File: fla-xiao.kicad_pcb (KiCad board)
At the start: 2 copper layers, 31 x 50 mm, 9 parts, among them J1 Conn_PinHeader_1x08_P2.54mm_V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, J2 Conn_PinHeader_1x04_P2.54mm_V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, J3 Conn_PinHeader_2x03_P2.54mm_V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, SW1 BUTTON_B3SN, U1 MOUDLE-SEEEDUINO-XIAO-ESP32C3

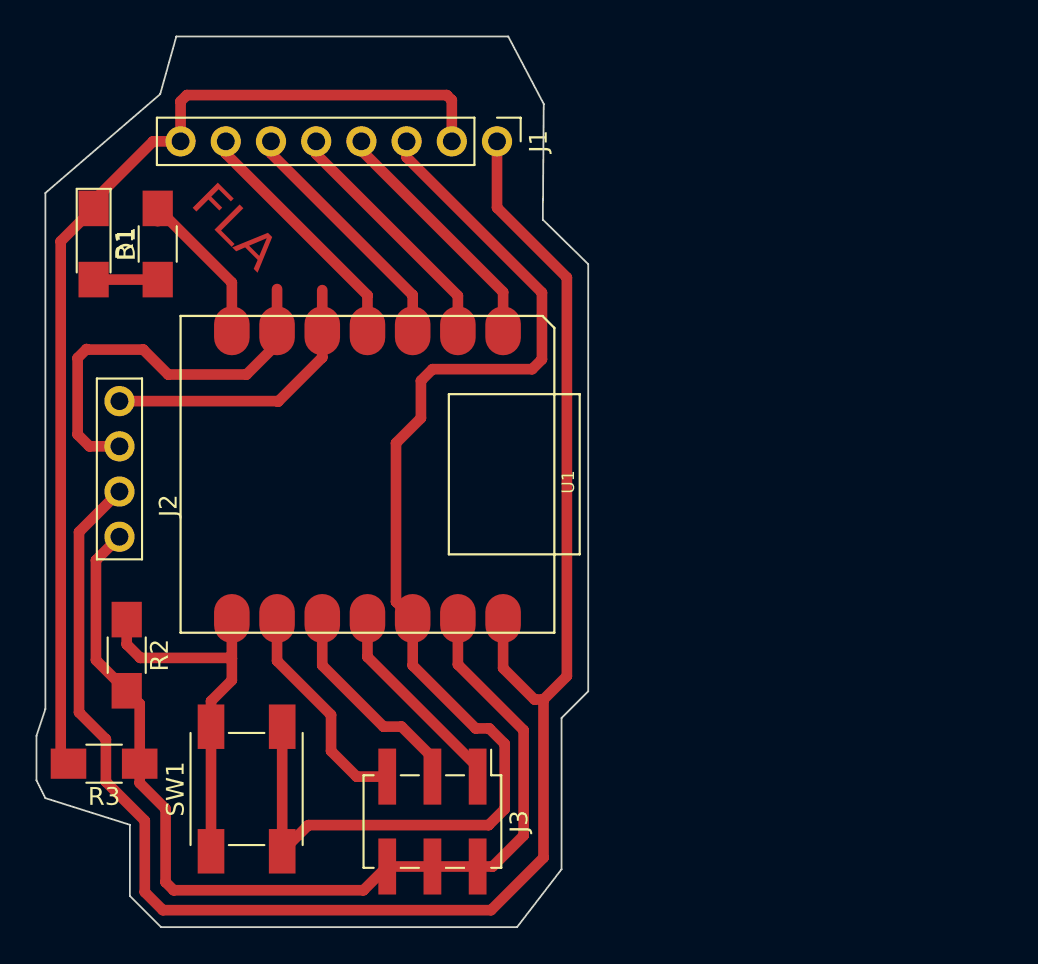
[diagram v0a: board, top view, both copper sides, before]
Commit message: Updated to use sockets with XIAO
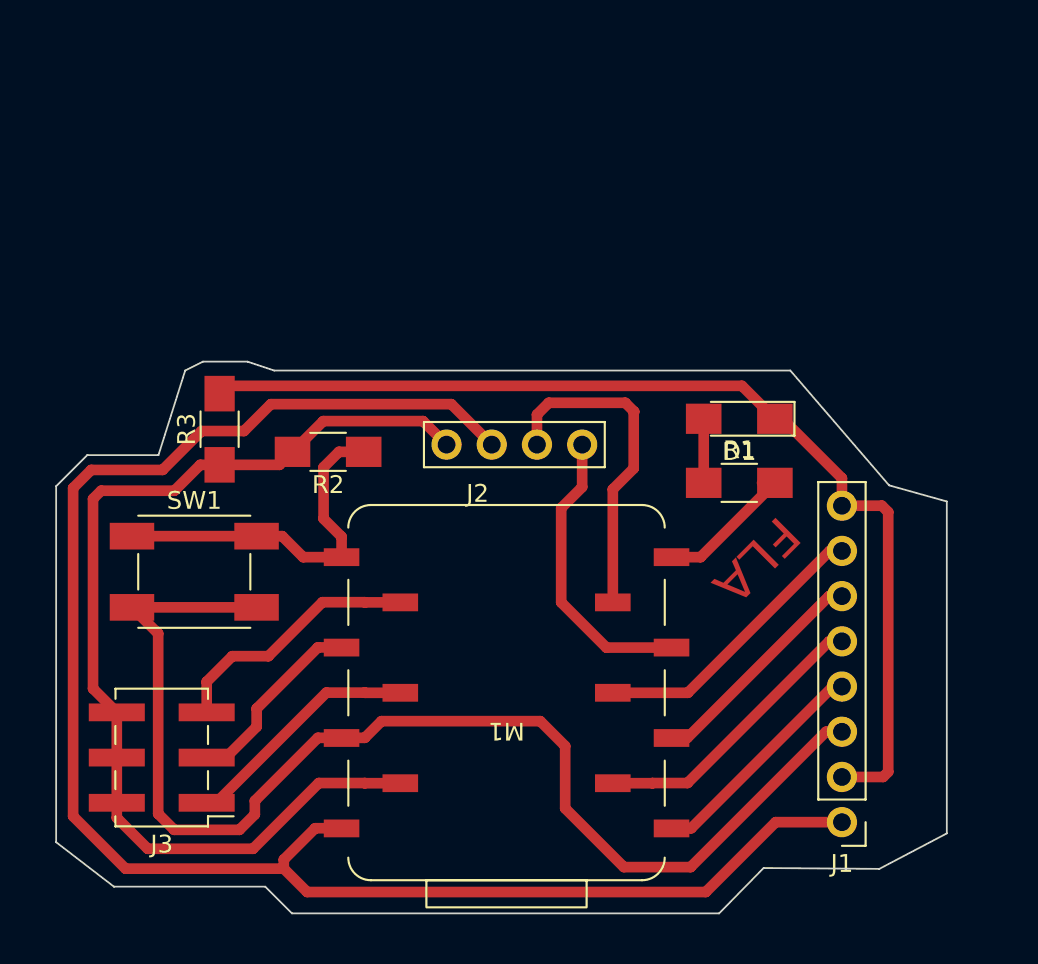
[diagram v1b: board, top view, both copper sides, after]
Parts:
- removed U1: MOUDLE-SEEEDUINO-XIAO-ESP32C3, xiao ESP32C3_PCB:MOUDLE14P-SMD-2.54-21X17.8MM
- added M1: Module_XIAO-RP2040_SocketSMD, fab:SeeedStudio_XIAO_SocketSMD, F.Cu at (148.2, 154.8)
- moved J1 42.9 mm to (167.0, 162.1), turned to 180 degrees
- moved D1 37.6 mm to (161.3, 139.4), turned to 180 degrees
- moved R1 35.3 mm to (161.3, 143.0), turned to 0 degrees
- moved J2 26.1 mm to (152.4, 140.9), turned to -90 degrees
- moved R3 19.9 mm to (132.1, 140.0), turned to 90 degrees
- moved R2 16.1 mm to (138.2, 141.3), turned to 180 degrees
- moved J3 15.6 mm to (128.8, 158.5), turned to 180 degrees
- moved SW1 12.6 mm to (130.6, 148.0), turned to 0 degrees
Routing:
- net Net-(J2-Pin_2): track 22.7 -> 18.8 mm
- net Net-(J1-Pin_5): track 13.9 -> 16.2 mm
- net Net-(J1-Pin_7): track 13.9 -> 16.2 mm
- net Net-(J3-Pin_5): track 12.5 -> 14.5 mm
- net Net-(J3-Pin_1): track 11.4 -> 13.4 mm
- net GND: track 115.8 -> 117.8 mm
- net Net-(J3-Pin_3): track 12.0 -> 10.7 mm
- net +5V: track 97.2 -> 95.9 mm
- net +3V3: track 70.8 -> 69.6 mm
- net Net-(M1-D6): track 9.32 -> 8.26 mm
- net Net-(J1-Pin_4): track 13.9 -> 12.9 mm
- net Net-(M1-D7): track 21.2 -> 20.3 mm
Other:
- board size 31 x 50 mm -> 50 x 31 mm

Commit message: .\fla-xiao.kicad*
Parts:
- moved R1 0.63 mm to (161.3, 142.4)
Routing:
- net Net-(D1-A): track 3.60 -> 2.97 mm

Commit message: Updated board
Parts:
- removed J1: Conn_PinHeader_1x08_P2.54mm_Vertical_THT_D1mm, fab:PinHeader_1x08_P2.54mm_Vertical_THT_D1mm
- removed J2: Conn_PinHeader_1x04_P2.54mm_Vertical_THT_D1mm, fab:PinHeader_1x04_P2.54mm_Vertical_THT_D1mm
- added J4: Conn_PinHeader_1x08_P2.54mm_Horizontal_SMD, fab:PinHeader_1x08_P2.54mm_Horizontal_SMD, F.Cu at (132.7, 147.6)
- added J5: Conn_PinHeader_1x05_P2.54mm_Horizontal_SMD, fab:PinHeader_1x05_P2.54mm_Horizontal_SMD, F.Cu at (155.6, 150.5)
- moved J3 47.8 mm to (169.5, 133.5), turned to 0 degrees
- moved SW1 39.3 mm to (169.7, 144.0)
- moved R3 38.1 mm to (168.3, 152.0), turned to -90 degrees
- moved D1 25.8 mm to (139.1, 152.6), turned to 0 degrees
- moved R2 25.8 mm to (162.2, 150.7)
- moved R1 23.3 mm to (139.1, 149.6), turned to 180 degrees
- moved M1 18.1 mm to (152.1, 137.2), turned to 0 degrees
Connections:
- net +3V3 renamed PWR_3V3
- net Net-(J3-Pin_1) renamed A10
- net Net-(J3-Pin_3) renamed A9
- net Net-(J3-Pin_5) renamed A8
- net Net-(M1-D6) renamed A6
- net Net-(M1-D7) renamed A7
- M1 pad 1: Net-(J1-Pin_4) -> A0
- M1 pad 14: +5V -> PWR_5V
- M1 pad 2: Net-(J1-Pin_5) -> A1
- M1 pad 3: Net-(J1-Pin_6) -> A2
- M1 pad 4: Net-(J1-Pin_7) -> A3
- M1 pad 5: Net-(J2-Pin_1) -> SDA
- M1 pad 6: Net-(J2-Pin_2) -> SCL
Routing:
- net +5V: track 96.0 -> 0.00 mm
- net PWR_5V: track 0.00 -> 54.0 mm
- net PWR_3V3: track 69.6 -> 113.3 mm
- net Net-(J2-Pin_2): track 18.8 -> 0.00 mm
- net A1: track 0.00 -> 16.7 mm
- net A3: track 0.00 -> 16.7 mm
- net Net-(J2-Pin_1): track 16.6 -> 0.00 mm
- net SDA: track 0.00 -> 16.4 mm
- net Net-(J1-Pin_5): track 16.2 -> 0.00 mm
- net Net-(J1-Pin_7): track 16.2 -> 0.00 mm
- net Net-(J1-Pin_6): track 13.6 -> 0.00 mm
- net A0: track 0.00 -> 13.4 mm
- net A2: track 0.00 -> 13.4 mm
- net Net-(J1-Pin_4): track 12.9 -> 0.00 mm
- net SCL: track 0.00 -> 8.98 mm
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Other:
- board size 50 x 31 mm -> 49.7 x 30.7 mm

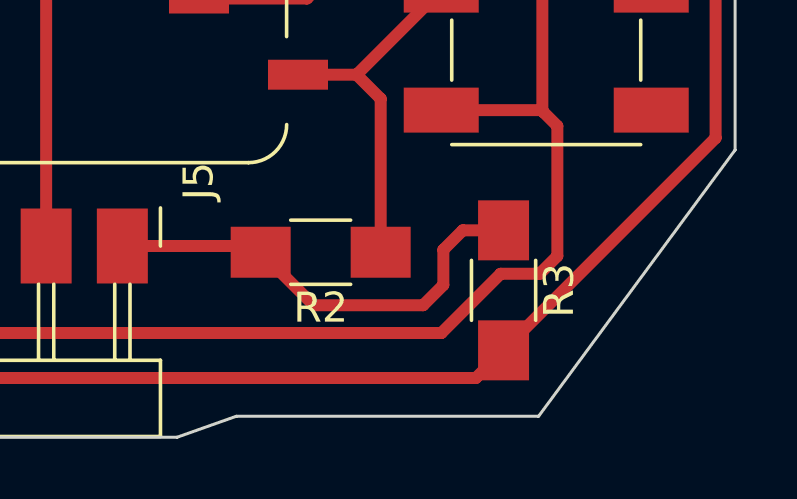
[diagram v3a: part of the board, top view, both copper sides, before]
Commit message: Updated images
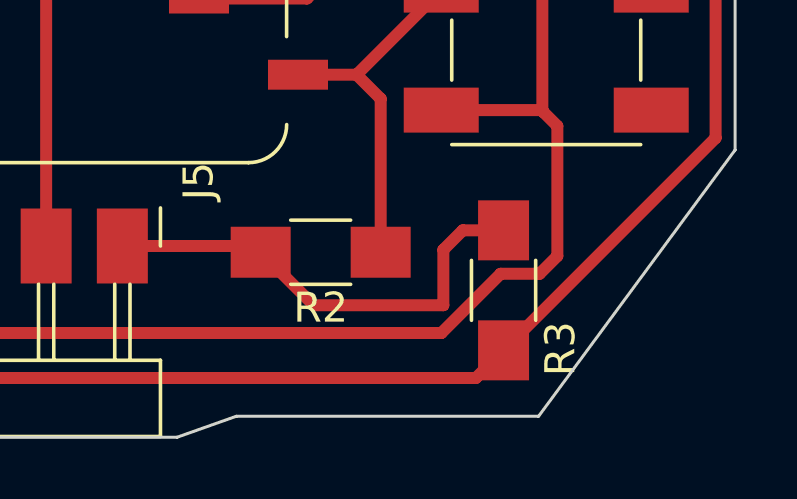
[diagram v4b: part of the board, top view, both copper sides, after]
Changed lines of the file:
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@@
     (property "ki_keywords" "R res resistor")
     (attr smd)
-    (fp_text reference "R3" (at 0 -1.85 90) (layer "F.SilkS")
-        (effects (font (size 1 1) (thickness 0.15)))
-    )
-    (fp_text value "R0" (at 0 1.9 90) (layer "F.Fab")
+    (fp_text reference "R3" (at 1.947049 -1.893203 90) (layer "F.SilkS")
+        (effects (font (size 1 1) (thickness 0.15)))
+    )
+    (fp_text value "R0" (at 0.172049 1.856797 90) (layer "F.Fab")
         (effects (font (size 1 1) (thickness 0.15)))
     )
@@
         (effects (font (size 1 1) (thickness 0.15)) (justify left))
     )
-    (fp_text value "Conn_PinHeader_1x05_P2.54mm_Horizontal_SMD" (at 0 13.335 90) (layer "F.Fab")
+    (fp_text value "Conn_PinHeader_1x05_P2.54mm_Horizontal_SMD" (at 7.8 3.95 -180) (layer "F.Fab")
         (effects (font (size 1 1) (thickness 0.15)))
     )
@@
   (segment (start 141.057596 152.565554) (end 141.057596 149.600355) (width 0.4) (layer "F.Cu") (net 1))
   (segment (start 159.952845 150.5) (end 160.160799 150.707954) (width 0.4) (layer "F.Cu") (net 2))
-  (segment (start 161.927845 152.475) (end 160.160799 150.707954) (width 0.4) (layer "F.Cu") (net 2))
-  (segment (start 165.575 152.475) (end 161.927845 152.475) (width 0.4) (layer "F.Cu") (net 2))
   (segment (start 132.7 149.875) (end 132.7 147.58) (width 0.4) (layer "F.Cu") (net 2))
   (segment (start 135.390554 152.565554) (end 132.7 149.875) (width 0.4) (layer "F.Cu") (net 2))
@@
   (segment (start 130.43 147.58) (end 132.7 147.58) (width 0.4) (layer "F.Cu") (net 2))
   (segment (start 160.175 128.025) (end 158.104797 130.095203) (width 0.4) (layer "F.Cu") (net 2))
-  (segment (start 166.25 150.625) (end 166.25 151.8) (width 0.4) (layer "F.Cu") (net 2))
+  (segment (start 166.897049 149.977951) (end 166.25 150.625) (width 0.4) (layer "F.Cu") (net 2))
   (segment (start 155.55 150.5) (end 159.952845 150.5) (width 0.4) (layer "F.Cu") (net 2))
   (segment (start 132.7 132.34) (end 128.96 132.34) (width 0.4) (layer "F.Cu") (net 2))
   (segment (start 172.05 130.975) (end 172.05 133.515) (width 0.4) (layer "F.Cu") (net 2))
+  (segment (start 161.927845 152.475) (end 160.160799 150.707954) (width 0.4) (layer "F.Cu") (net 2))
   (segment (start 137.057596 152.565554) (end 135.390554 152.565554) (width 0.4) (layer "F.Cu") (net 2))
-  (segment (start 168.256797 149.977951) (end 166.897049 149.977951) (width 0.4) (layer "F.Cu") (net 2))
+  (segment (start 166.25 150.625) (end 166.25 152.475) (width 0.4) (layer "F.Cu") (net 2))
   (segment (start 137.057596 153.282596) (end 137.057596 152.565554) (width 0.4) (layer "F.Cu") (net 2))
   (segment (start 175.325 146.9) (end 168.256797 153.968203) (width 0.4) (layer "F.Cu") (net 2))
   (segment (start 172.05 130.15) (end 169.925 128.025) (width 0.4) (layer "F.Cu") (net 2))
-  (segment (start 166.897049 149.977951) (end 166.25 150.625) (width 0.4) (layer "F.Cu") (net 2))
   (segment (start 172.05 130.975) (end 172.05 130.15) (width 0.4) (layer "F.Cu") (net 2))
   (segment (start 169.925 128.025) (end 160.175 128.025) (width 0.4) (layer "F.Cu") (net 2))
   (segment (start 128.96 132.34) (end 128.3 133) (width 0.4) (layer "F.Cu") (net 2))
-  (segment (start 166.25 151.8) (end 165.575 152.475) (width 0.4) (layer "F.Cu") (net 2))
+  (segment (start 168.256797 149.977951) (end 166.897049 149.977951) (width 0.4) (layer "F.Cu") (net 2))
   (segment (start 138.675 154.9) (end 137.057596 153.282596) (width 0.4) (layer "F.Cu") (net 2))
   (segment (start 168.256797 153.968203) (end 168.256797 153.977951) (width 0.4) (layer "F.Cu") (net 2))
   (segment (start 172.05 136.65) (end 175.325 139.925) (width 0.4) (layer "F.Cu") (net 2))
+  (segment (start 166.25 152.475) (end 161.927845 152.475) (width 0.4) (layer "F.Cu") (net 2))
   (segment (start 172.05 136.055) (end 172.05 136.65) (width 0.4) (layer "F.Cu") (net 2))
   (segment (start 168.256802 149.977954) (end 168.256798 149.977951) (width 0.6) (layer "F.Cu") (net 2))
